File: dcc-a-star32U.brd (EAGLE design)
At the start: 31.7 x 17.8 mm, 9 parts, among them Q1 MOSFET-NCHANNEL2N7002PW

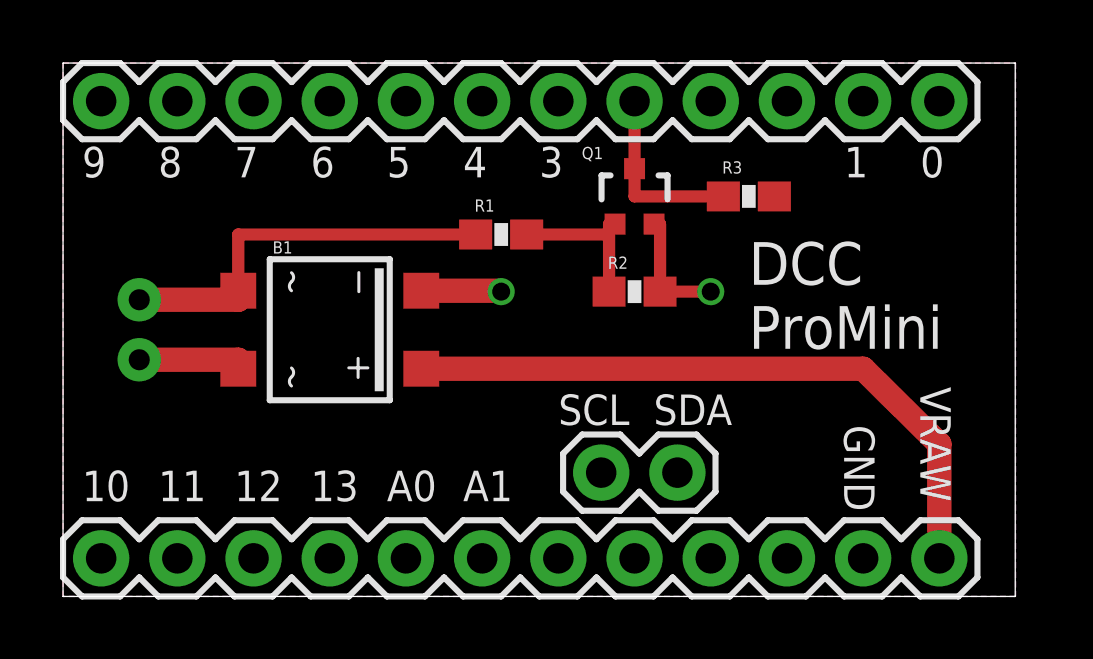
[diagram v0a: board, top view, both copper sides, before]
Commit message: add a-star variant, use JST for dcc-powered boards
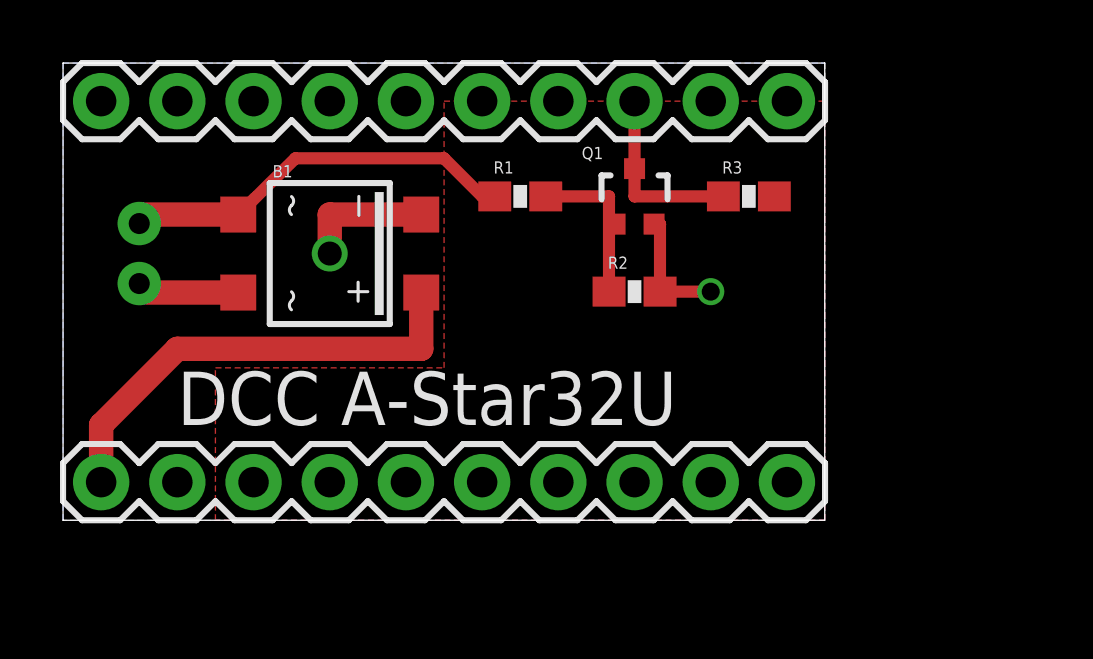
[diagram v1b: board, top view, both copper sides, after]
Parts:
- removed JP3: M02PTH, SparkFun-Connectors:1X02
- JP1, JP2: value M12PTH -> M10"; device SparkFun-Connectors:1X12 -> SparkFun-Connectors:1X10
- moved JP1 27.9 mm to (1.27, 16.5), turned to 0 degrees
- moved JP2 2.54 mm to (1.27, 3.81)
- moved B1 2.54 mm to (8.89, 11.4)
- moved DCC-IN 2.54 mm to (2.54, 11.4)
- moved R1 1.42 mm to (15.2, 13.3)
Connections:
- removed net SCL: JP3.2
- removed net SDA: JP3.1
- net 5V: now also JP2.3; no longer JP2.9
- net DCC-INT: now also JP1.8; no longer JP1.5
- net GND: now also JP2.2; no longer JP1.4, JP2.11
- net VRAW: now also JP2.1; no longer JP2.12
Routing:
- net VRAW: track 22.1 -> 15.5 mm
- net GND: track 6.84 -> 8.49 mm
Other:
- board size 31.7 x 17.8 mm -> 25.4 x 15.2 mm
- board text added: "DCC A-Star32U"
- board text removed: "0"
- board text removed: "1"
- board text removed: "10"
- board text removed: "11"
- board text removed: "12"
- board text removed: "13"
- board text removed: "3"
- board text removed: "4"
- board text removed: "5"
- board text removed: "6"
- board text removed: "7"
- board text removed: "8"
- board text removed: "9"
- board text removed: "A0"
- board text removed: "A1"
- board text removed: "DCC ProMini"
- board text removed: "GND"
- board text removed: "SCL"
- board text removed: "SDA"
- board text removed: "VRAW"
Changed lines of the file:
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@@
 <board>
 <plain>
-<wire x1="0" y1="17.78" x2="0" y2="0" width="0" layer="20"/>
-<wire x1="0" y1="0" x2="31.74" y2="0" width="0" layer="20"/>
-<wire x1="31.74" y1="0" x2="31.74" y2="17.78" width="0" layer="20"/>
-<wire x1="31.74" y1="17.78" x2="0" y2="17.78" width="0" layer="20"/>
-<text x="22.86" y="8.255" size="1.4224" layer="21" font="vector" ratio="9">DCC
-ProMini</text>
-<text x="28.575" y="6.985" size="1.016" layer="21" rot="SR270">VRAW</text>
-<text x="26.035" y="5.715" size="1.016" layer="21" rot="SR270">GND</text>
-<text x="16.51" y="5.715" size="1.016" layer="21" rot="SR0">SCL</text>
-<text x="19.685" y="5.715" size="1.016" layer="21" rot="SR0">SDA</text>
-<text x="28.575" y="13.97" size="1.016" layer="21" rot="SR0">0</text>
-<text x="26.035" y="13.97" size="1.016" layer="21" rot="SR0">1</text>
-<text x="15.875" y="13.97" size="1.016" layer="21" rot="SR0">3</text>
-<text x="13.335" y="13.97" size="1.016" layer="21" rot="SR0">4</text>
-<text x="10.795" y="13.97" size="1.016" layer="21" rot="SR0">5</text>
-<text x="8.255" y="13.97" size="1.016" layer="21" rot="SR0">6</text>
-<text x="5.715" y="13.97" size="1.016" layer="21" rot="SR0">7</text>
-<text x="3.175" y="13.97" size="1.016" layer="21" rot="SR0">8</text>
-<text x="0.635" y="13.97" size="1.016" layer="21" rot="SR0">9</text>
-<text x="0.635" y="3.175" size="1.016" layer="21" rot="SR0">10</text>
-<text x="3.175" y="3.175" size="1.016" layer="21" rot="SR0">11</text>
-<text x="5.715" y="3.175" size="1.016" layer="21" rot="SR0">12</text>
-<text x="8.255" y="3.175" size="1.016" layer="21" rot="SR0">13</text>
-<text x="10.795" y="3.175" size="1.016" layer="21" rot="SR0">A0</text>
-<text x="13.335" y="3.175" size="1.016" layer="21" rot="SR0">A1</text>
+<wire x1="0" y1="17.78" x2="0" y2="2.54" width="0" layer="20"/>
+<wire x1="0" y1="2.54" x2="25.39" y2="2.54" width="0" layer="20"/>
+<wire x1="25.39" y1="2.54" x2="25.39" y2="17.78" width="0" layer="20"/>
+<wire x1="25.39" y1="17.78" x2="0" y2="17.78" width="0" layer="20"/>
+<text x="3.81" y="5.715" size="1.778" layer="21" font="vector">DCC A-Star32U</text>
 </plain>
 <attributes>
@@
 </autorouter>
 <elements>
-<element name="DCC-IN" library="SparkFun-Connectors" package="JST-2-PTH-NS" value="M02-JST-2-PTH-NO_SILK" x="2.54" y="8.89" smashed="yes" rot="R90"/>
-<element name="B1" library="rectifier" package="SOIC-4" value="MB1S" x="8.89" y="8.89" smashed="yes" rot="R270">
-<attribute name="NAME" x="6.985" y="11.43" size="0.4064" layer="25" font="vector"/>
+<element name="DCC-IN" library="SparkFun-Connectors" package="JST-2-PTH-NS" value="M02-JST-2-PTH-NO_SILK" x="2.54" y="11.43" smashed="yes" rot="R90"/>
+<element name="B1" library="rectifier" package="SOIC-4" value="MB1S" x="8.89" y="11.43" smashed="yes" rot="R270">
+<attribute name="NAME" x="6.985" y="13.97" size="0.4064" layer="25" font="vector"/>
 </element>
-<element name="R1" library="SparkFun-Passives" package="0603-RES" value="47K" x="14.605" y="12.065"/>
+<element name="R1" library="SparkFun-Passives" package="0603-RES" value="47K" x="15.24" y="13.335"/>
 <element name="Q1" library="SparkFun-DiscreteSemi" package="SOT323" value="MOSFET-NCHANNEL2N7002PW" x="19.05" y="13.335" smashed="yes">
 <attribute name="PROD_ID" value="TRANS-11151" x="19.05" y="13.335" size="0.4064" layer="27" display="off"/>
@@
 <element name="R3" library="SparkFun-Passives" package="0603-RES" value="10K" x="22.86" y="13.335"/>
 <element name="R2" library="SparkFun-Passives" package="0603-RES" value="100K" x="19.05" y="10.16"/>
-<element name="JP1" library="SparkFun-Connectors" package="1X12" value="M12PTH" x="29.21" y="16.51" smashed="yes" rot="R180"/>
-<element name="JP2" library="SparkFun-Connectors" package="1X12" value="M12PTH" x="1.27" y="1.27" smashed="yes"/>
-<element name="JP3" library="SparkFun-Connectors" package="1X02" value="M02PTH" x="17.93875" y="4.1275" smashed="yes"/>
+<element name="JP1" library="SparkFun-Connectors" package="1X10" value="M10&quot;" x="1.27" y="16.51" smashed="yes"/>
+<element name="JP2" library="SparkFun-Connectors" package="1X10" value="M10&quot;" x="1.27" y="3.81" smashed="yes"/>
 </elements>
 <signals>
@@
 <polygon width="0.4064" layer="16" isolate="0.3048">
 <vertex x="0" y="17.78"/>
-<vertex x="31.75" y="17.78"/>
-<vertex x="31.75" y="0"/>
-<vertex x="0" y="0"/>
+<vertex x="25.4" y="17.78"/>
+<vertex x="25.4" y="2.54"/>
+<vertex x="0" y="2.54"/>
 </polygon>
 <contactref element="B1" pad="-"/>
@@
 <wire x1="19.9" y1="10.16" x2="21.59" y2="10.16" width="0.4064" layer="1"/>
 <via x="21.59" y="10.16" extent="1-16" drill="0.6" shape="square"/>
-<wire x1="11.94" y1="10.19" x2="14.605" y2="10.19" width="0.8128" layer="1"/>
-<wire x1="14.605" y1="10.19" x2="14.605" y2="10.16" width="0.8128" layer="1"/>
-<via x="14.605" y="10.16" extent="1-16" drill="0.6" shape="square"/>
-<contactref element="JP1" pad="4"/>
-<contactref element="JP2" pad="11"/>
+<wire x1="11.94" y1="12.73" x2="8.89" y2="12.73" width="0.8128" layer="1"/>
+<wire x1="8.89" y1="12.73" x2="8.89" y2="11.43" width="0.8128" layer="1"/>
+<via x="8.89" y="11.43" extent="1-16" drill="0.8" shape="square"/>
+<contactref element="JP2" pad="2"/>
 </signal>
 <signal name="DCC-INT">
@@
 <wire x1="19.05" y1="14.26" x2="19.05" y2="13.335" width="0.4064" layer="1"/>
 <wire x1="19.05" y1="13.335" x2="22.01" y2="13.335" width="0.4064" layer="1"/>
-<wire x1="19.05" y1="16.51" x2="19.05" y2="14.26" width="0.4064" layer="1"/>
-<contactref element="JP1" pad="5"/>
+<contactref element="JP1" pad="8"/>
+<wire x1="19.05" y1="14.26" x2="19.05" y2="16.51" width="0.4064" layer="1"/>
 </signal>
 <signal name="5V">
 <polygon width="0.4064" layer="1" isolate="0.3048">
-<vertex x="0" y="17.78"/>
-<vertex x="31.75" y="17.78"/>
-<vertex x="31.75" y="0"/>
-<vertex x="0" y="0"/>
+<vertex x="12.7" y="16.51"/>
+<vertex x="25.4" y="16.51"/>
+<vertex x="25.4" y="2.54"/>
+<vertex x="5.08" y="2.54"/>
+<vertex x="5.08" y="7.62"/>
+<vertex x="12.7" y="7.62"/>
 </polygon>
 <contactref element="R3" pad="2"/>
-<contactref element="JP2" pad="9"/>
+<contactref element="JP2" pad="3"/>
 </signal>
 <signal name="VRAW">
 <contactref element="B1" pad="+"/>
-<wire x1="11.94" y1="7.59" x2="26.67" y2="7.59" width="0.8128" layer="1"/>
-<wire x1="26.67" y1="7.59" x2="29.21" y2="5.08" width="0.8128" layer="1"/>
-<wire x1="29.21" y1="5.08" x2="29.21" y2="1.27" width="0.8128" layer="1"/>
-<contactref element="JP2" pad="12"/>
+<contactref element="JP2" pad="1"/>
+<wire x1="11.94" y1="8.255" x2="3.81" y2="8.255" width="0.8128" layer="1"/>
+<wire x1="3.81" y1="8.255" x2="1.27" y2="5.715" width="0.8128" layer="1"/>
+<wire x1="1.27" y1="5.715" x2="1.27" y2="3.81" width="0.8128" layer="1"/>
+<wire x1="11.94" y1="8.255" x2="11.94" y2="10.13" width="0.8128" layer="1"/>
 </signal>
 <signal name="N$3">
@@
 <contactref element="DCC-IN" pad="2"/>
 <contactref element="R1" pad="1"/>
-<wire x1="13.755" y1="12.065" x2="5.84" y2="12.065" width="0.4064" layer="1"/>
-<wire x1="5.84" y1="12.065" x2="5.84" y2="10.19" width="0.4064" layer="1"/>
-<wire x1="2.54" y1="9.89" x2="5.84" y2="9.89" width="0.8128" layer="1"/>
-<wire x1="5.84" y1="9.89" x2="5.84" y2="10.19" width="0.8128" layer="1"/>
+<wire x1="14.39" y1="13.335" x2="13.97" y2="13.335" width="0.4064" layer="1"/>
+<wire x1="13.97" y1="13.335" x2="12.7" y2="14.605" width="0.4064" layer="1"/>
+<wire x1="12.7" y1="14.605" x2="7.745" y2="14.605" width="0.4064" layer="1"/>
+<wire x1="7.745" y1="14.605" x2="5.84" y2="12.73" width="0.4064" layer="1"/>
+<wire x1="5.84" y1="12.73" x2="2.57" y2="12.73" width="0.8128" layer="1"/>
+<wire x1="2.57" y1="12.73" x2="2.54" y2="12.43" width="0.8128" layer="1"/>
 </signal>
 <signal name="N$4">
 <contactref element="B1" pad="~2"/>
 <contactref element="DCC-IN" pad="1"/>
-<wire x1="2.54" y1="7.89" x2="5.84" y2="7.89" width="0.8128" layer="1"/>
-<wire x1="5.84" y1="7.89" x2="5.84" y2="7.59" width="0.8128" layer="1"/>
+<wire x1="5.84" y1="10.13" x2="2.51" y2="10.13" width="0.8128" layer="1"/>
+<wire x1="2.51" y1="10.13" x2="2.54" y2="10.43" width="0.8128" layer="1"/>
 </signal>
 <signal name="N$1">
@@
 <contactref element="Q1" pad="1"/>
 <contactref element="R2" pad="1"/>
-<wire x1="15.455" y1="12.065" x2="18.2" y2="12.065" width="0.4064" layer="1"/>
-<wire x1="18.2" y1="12.41" x2="18.2" y2="12.065" width="0.4064" layer="1"/>
-<wire x1="18.2" y1="12.065" x2="18.2" y2="10.16" width="0.4064" layer="1"/>
+<wire x1="16.09" y1="13.335" x2="18.2" y2="13.335" width="0.4064" layer="1"/>
+<wire x1="18.2" y1="13.335" x2="18.2" y2="12.41" width="0.4064" layer="1"/>
+<wire x1="18.2" y1="12.41" x2="18.2" y2="10.16" width="0.4064" layer="1"/>
 <wire x1="18.4" y1="12.41" x2="18.2" y2="12.41" width="0.4064" layer="1"/>
-</signal>
-<signal name="SCL">
-<contactref element="JP3" pad="2"/>
-</signal>
-<signal name="SDA">
-<contactref element="JP3" pad="1"/>
 </signal>
 </signals>
 </board>
 </drawing>
-<compatibility>
-<note version="6.3" minversion="6.2.2" severity="warning">
-Since Version 6.2.2 text objects can contain more than one line,
-which will not be processed correctly with this version.
-</note>
-</compatibility>
 </eagle>
